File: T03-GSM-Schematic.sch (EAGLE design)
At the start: 19 parts, among them IC1 788TV, J1 POWER_JACKPTH_BREAD, J2 AVR, Q2 16M, U1 ATMEGA328P-PU

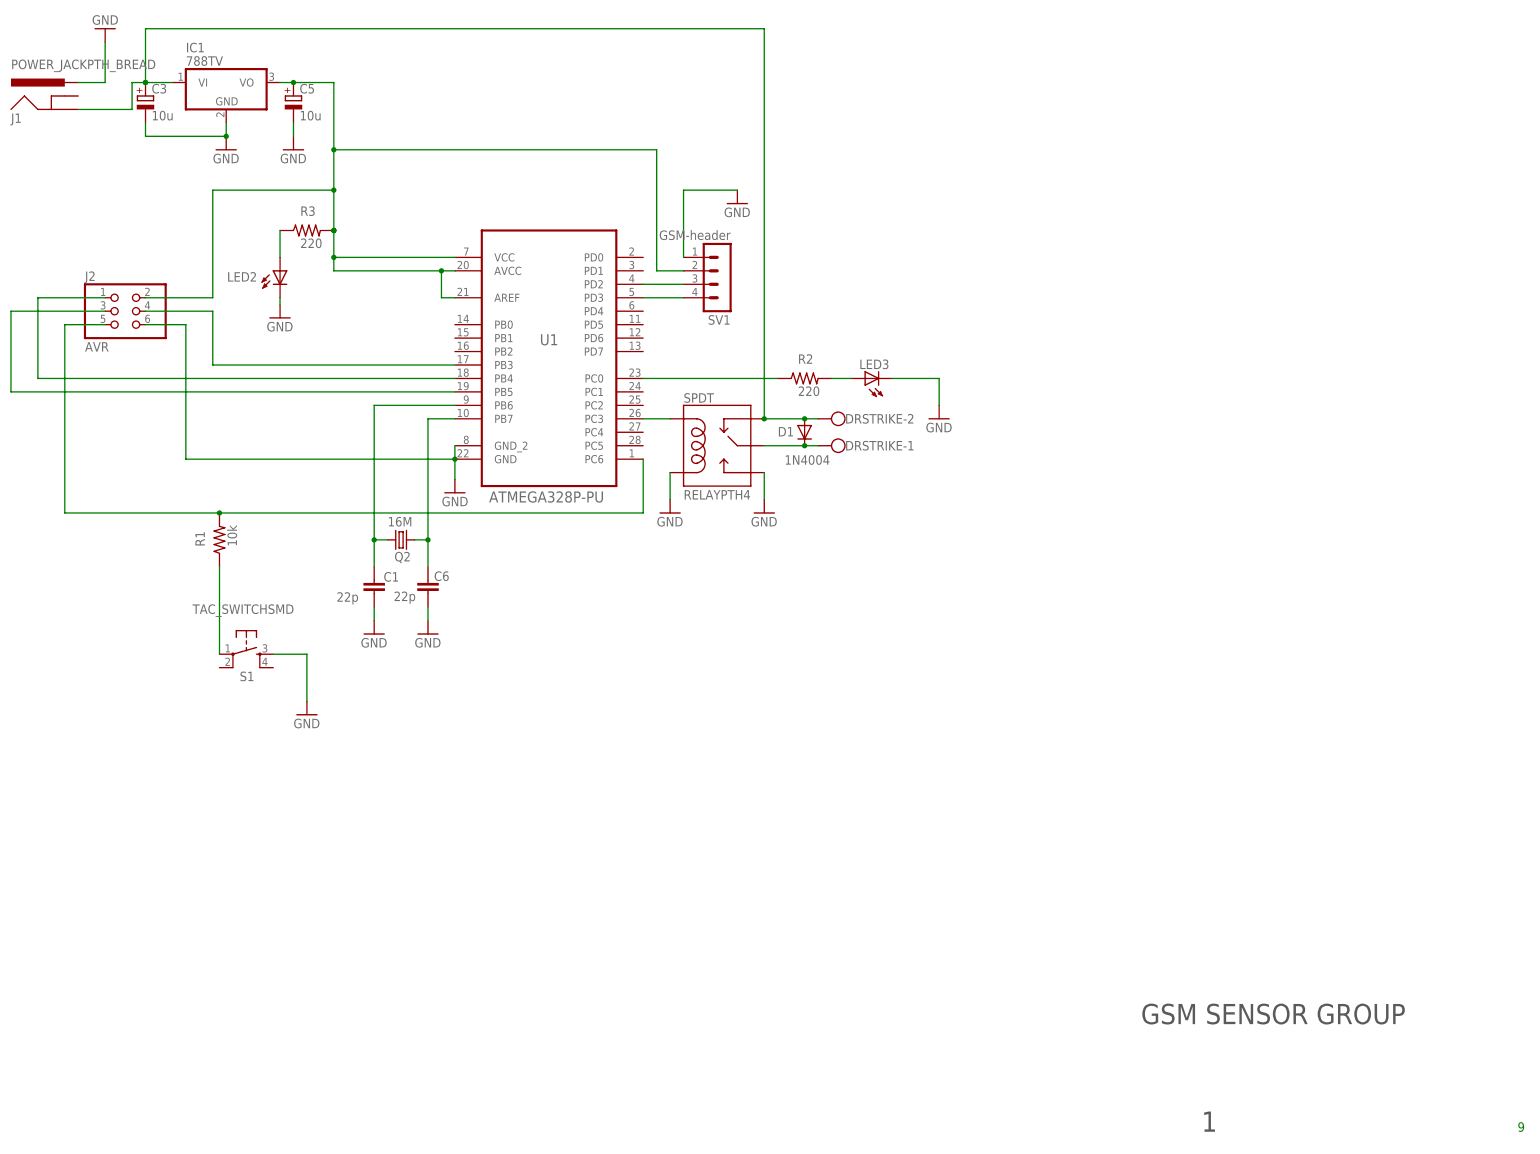
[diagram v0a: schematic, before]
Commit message: Add files via upload
Fixed power jack pin on schematic. There is an inconsistency with the board and schematic
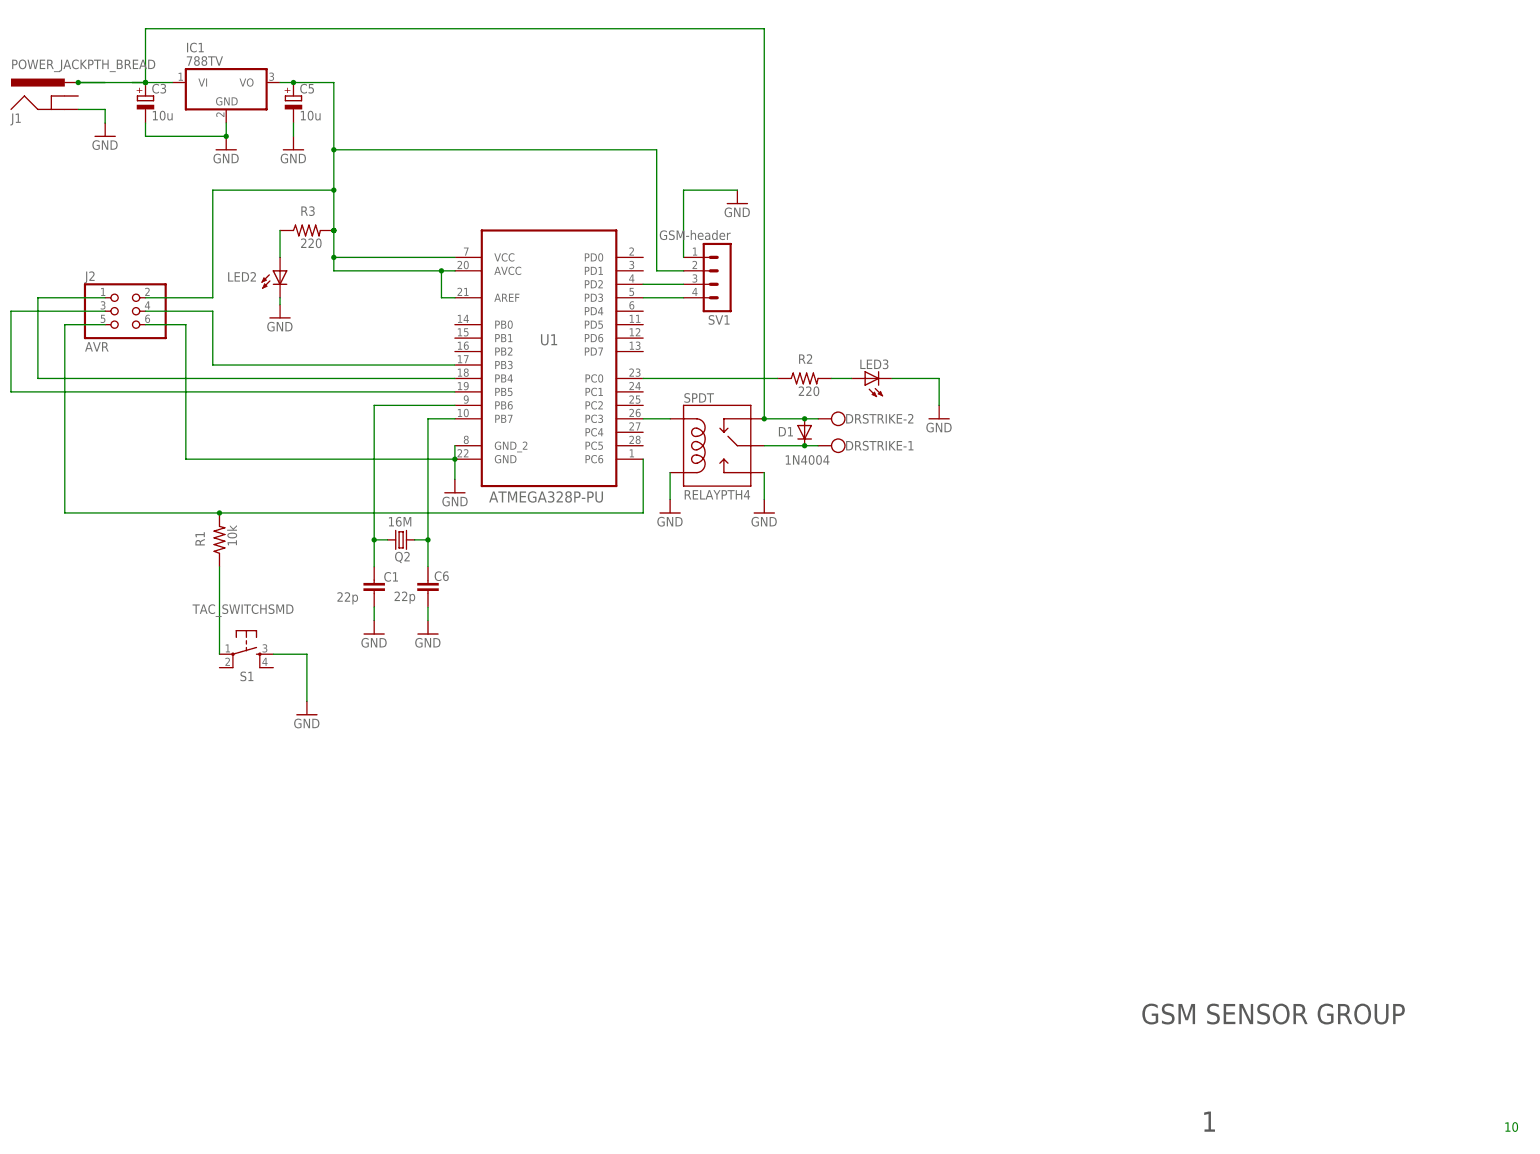
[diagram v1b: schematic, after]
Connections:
- net 12V: now also J1.PWR; no longer J1.GND
- net GND: now also J1.GND; no longer J1.PWR
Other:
- note added: "10"
- note removed: "9"
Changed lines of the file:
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@@
 <part name="GND6" library="supply1" deviceset="GND" device=""/>
 <part name="J1" library="SparkFun-Connectors" deviceset="POWER_JACK" device="PTH_BREAD" value="POWER_JACKPTH_BREAD"/>
-<part name="GND7" library="supply1" deviceset="GND" device=""/>
 <part name="FRAME1" library="frames" deviceset="FRAME_B_L" device=""/>
 <part name="R3" library="rcl" deviceset="R-US_" device="R0603" value="220"/>
@@
 <part name="SV1" library="con-lstb" deviceset="MA04-1" device="" value="GSM-header"/>
 <part name="GND12" library="supply1" deviceset="GND" device=""/>
+<part name="GND7" library="supply1" deviceset="GND" device=""/>
 </parts>
 <sheets>
@@
 <text x="359.41" y="7.62" size="3.81" layer="97" font="vector">1</text>
 <text x="347.98" y="27.94" size="3.81" layer="97" font="vector">GSM SENSOR GROUP</text>
-<text x="419.1" y="7.62" size="1.778" layer="91">9</text>
+<text x="416.56" y="7.62" size="1.778" layer="91">10</text>
 </plain>
 <instances>
@@
 <instance part="GND6" gate="1" x="190.5" y="86.36"/>
 <instance part="J1" gate="G$1" x="144.78" y="198.12"/>
-<instance part="GND7" gate="1" x="152.4" y="215.9" rot="R180"/>
 <instance part="FRAME1" gate="G$1" x="0" y="0"/>
 <instance part="FRAME1" gate="G$2" x="325.12" y="0"/>
@@
 <instance part="SV1" gate="1" x="269.24" y="167.64" rot="R180"/>
 <instance part="GND12" gate="1" x="271.78" y="182.88"/>
+<instance part="GND7" gate="1" x="152.4" y="195.58"/>
 </instances>
 <busses>
@@
 </segment>
 <segment>
-<pinref part="GND7" gate="1" pin="GND"/>
-<wire x1="152.4" y1="213.36" x2="152.4" y2="205.74" width="0.1524" layer="91"/>
-<wire x1="152.4" y1="205.74" x2="147.32" y2="205.74" width="0.1524" layer="91"/>
-<pinref part="J1" gate="G$1" pin="PWR"/>
-</segment>
-<segment>
 <pinref part="SV1" gate="1" pin="1"/>
 <wire x1="261.62" y1="172.72" x2="261.62" y2="185.42" width="0.1524" layer="91"/>
 <pinref part="GND12" gate="1" pin="GND"/>
 <wire x1="261.62" y1="185.42" x2="271.78" y2="185.42" width="0.1524" layer="91"/>
+</segment>
+<segment>
+<pinref part="J1" gate="G$1" pin="GND"/>
+<pinref part="GND7" gate="1" pin="GND"/>
+<wire x1="147.32" y1="200.66" x2="152.4" y2="200.66" width="0.1524" layer="91"/>
+<wire x1="152.4" y1="200.66" x2="152.4" y2="198.12" width="0.1524" layer="91"/>
 </segment>
 </net>
@@
 <wire x1="284.48" y1="142.24" x2="276.86" y2="142.24" width="0.1524" layer="91"/>
 <junction x="284.48" y="142.24"/>
-<wire x1="157.48" y1="200.66" x2="157.48" y2="205.74" width="0.1524" layer="91"/>
 <wire x1="157.48" y1="205.74" x2="160.02" y2="205.74" width="0.1524" layer="91"/>
-<pinref part="J1" gate="G$1" pin="GND"/>
-<wire x1="157.48" y1="200.66" x2="147.32" y2="200.66" width="0.1524" layer="91"/>
 <pinref part="IC1" gate="A1" pin="VI"/>
-</segment>
-</net>
+<wire x1="152.4" y1="205.74" x2="147.32" y2="205.74" width="0.1524" layer="91"/>
+<pinref part="J1" gate="G$1" pin="PWR"/>
+<wire x1="160.02" y1="205.74" x2="147.32" y2="205.74" width="0.1524" layer="91"/>
+<junction x="147.32" y="205.74"/>
+</segment>
+</net>
